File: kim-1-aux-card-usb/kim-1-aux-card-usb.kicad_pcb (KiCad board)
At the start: 2 copper layers, 64.3 x 110.7 mm, 36 parts, among them J1 Motherboard, J2 SD_Shield, J3 DIN-6, J4 Reset, J5 GND, J6 +5V, J7 USB_C_Receptacle_USB2.0, J8 USB_TTL, J9 TTL_SERIAL, Q1 PN2222A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

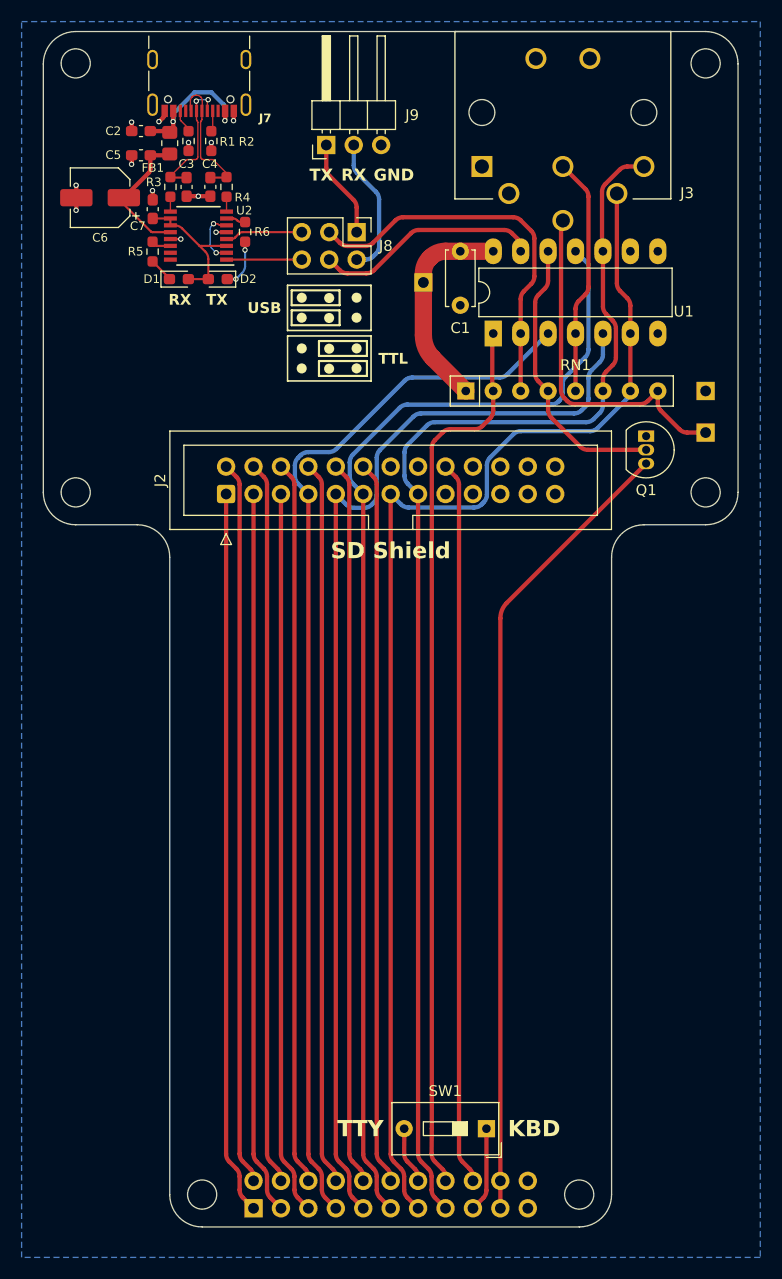
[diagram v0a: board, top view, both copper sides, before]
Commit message: Revision 3. Fixes Issue #3
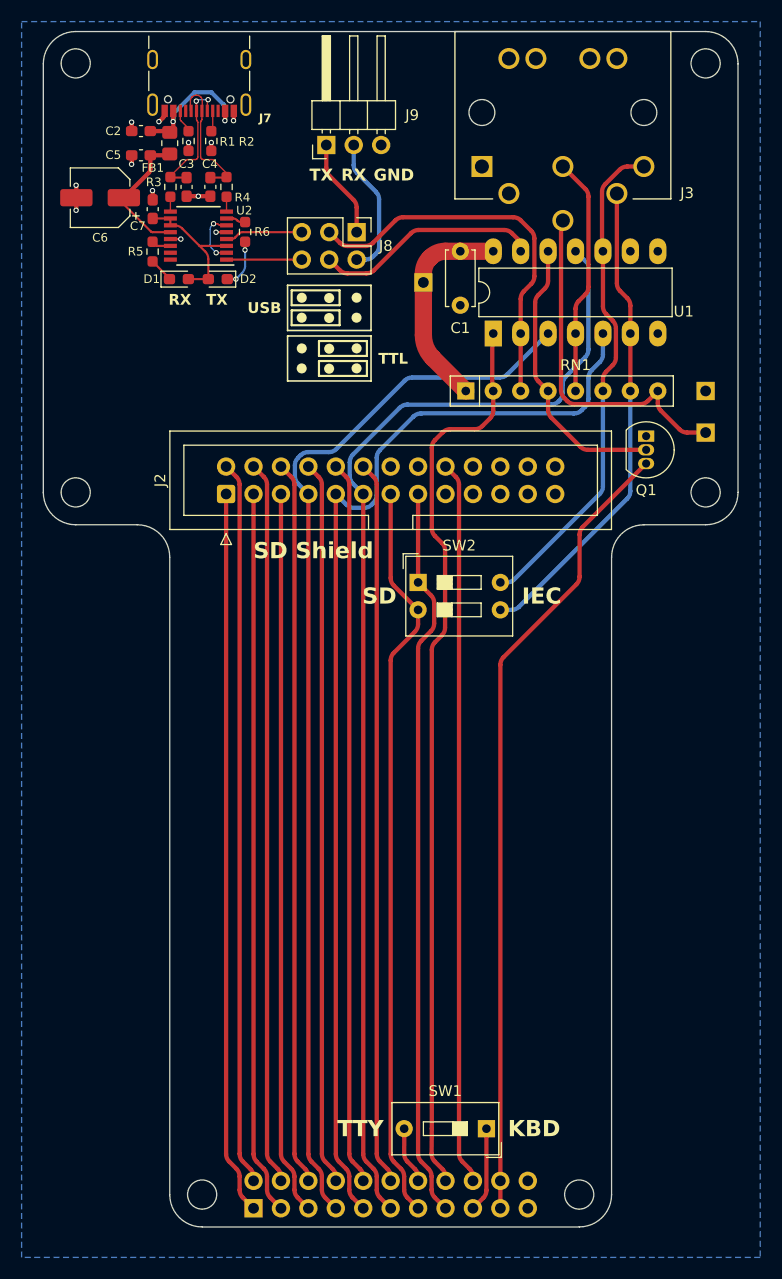
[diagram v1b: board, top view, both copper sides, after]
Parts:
- added SW2: SD_IEC, Button_Switch_THT:SW_DIP_SPSTx02_Slide_9.78x7.26mm_W7.62mm_P2.54mm, F.Cu at (144.5, 91.1)
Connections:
- J3 pad 4: /PA6 -> Net-(RN1F-R6.2)
- J3 pad 5: /PA7 -> Net-(RN1E-R5.2)
- RN1 pad 6: /PA7 -> Net-(RN1E-R5.2)
- RN1 pad 7: /PA6 -> Net-(RN1F-R6.2)
- U1 pad 10: /PA7 -> Net-(RN1E-R5.2)
- U1 pad 6: /PA6 -> Net-(RN1F-R6.2)
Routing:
- net /PA7: track 117.5 -> 68.1 mm
- net Net-(RN1E-R5.2): track 0.00 -> 46.4 mm
- net /PA6: track 115.0 -> 69.0 mm
- net Net-(RN1F-R6.2): track 0.00 -> 44.8 mm
- net /PTR: track 82.9 -> 83.7 mm
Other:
- board text added: "IEC"
- board text added: "SD"
